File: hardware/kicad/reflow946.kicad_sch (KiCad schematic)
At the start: 47 parts, among them J1 VH-2A, J2 VH-3A2, J3 VH-3A2, J4 XH-A2, J5 HDR-M-2.54_2x3, Q1 BTA16-600BRG, Q2 MMBT3906, Q3 MMBT3906, Q4 MMBT3906, SW1 SW_Push, SW2 SW_Push, SW3 SW_Push, U1 MOC3041M, U2 ESP32-WROOM-32U, U3 MAX31855KASA, U4 AMS1117-3.3

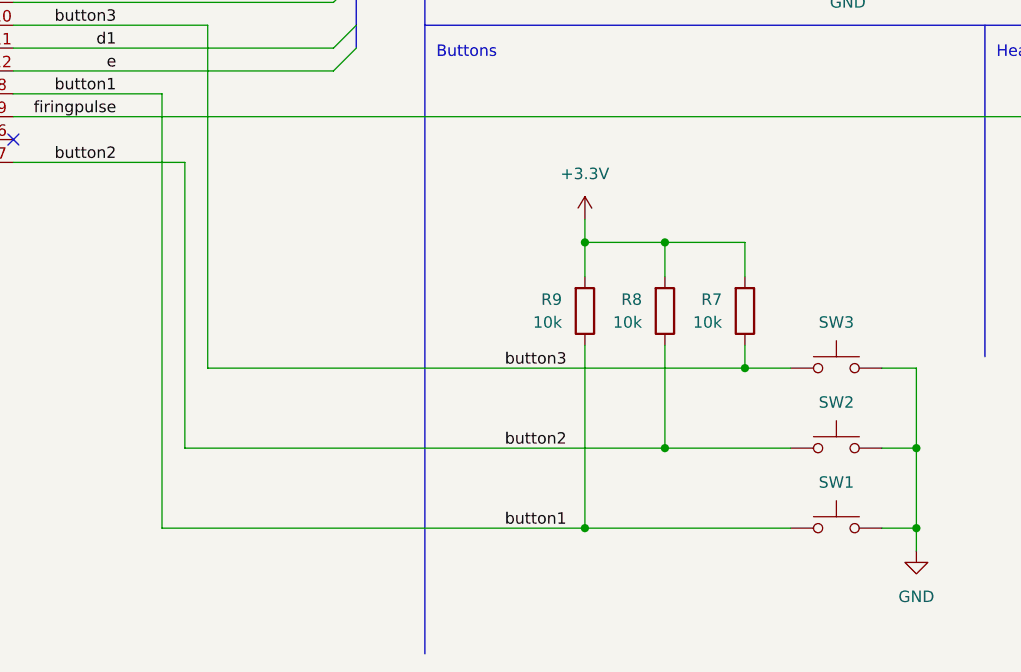
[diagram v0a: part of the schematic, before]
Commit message: Fix wrong pinout on push buttons
Leaving pull up resistor footprints in place, so they can be populated
if needed.
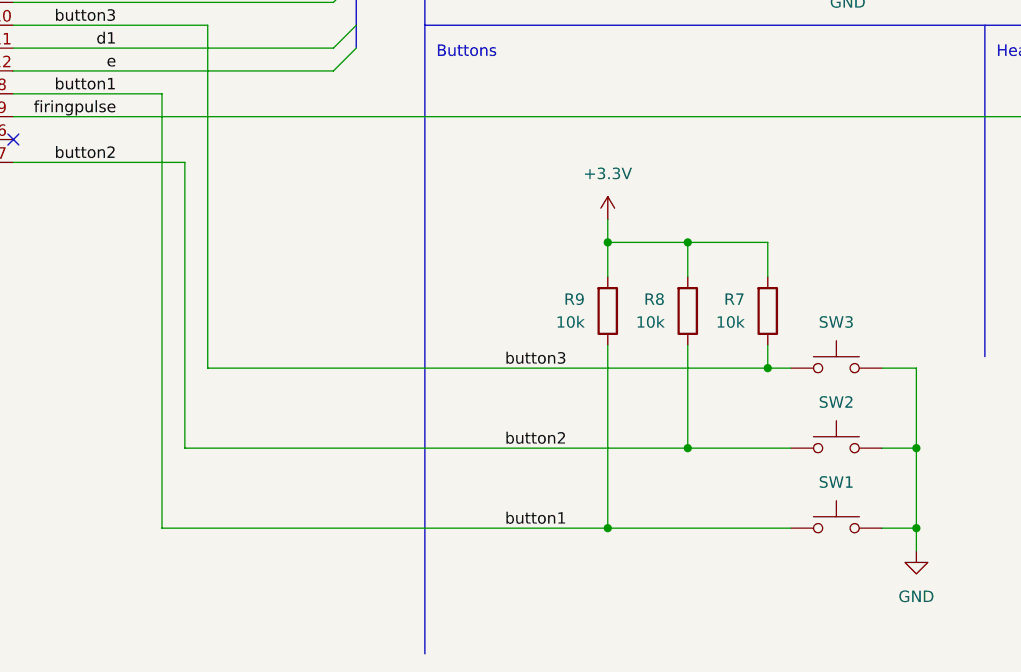
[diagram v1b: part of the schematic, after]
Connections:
- net GND: now also SW1.2, SW2.2, SW3.2; no longer SW1.1, SW2.1, SW3.1
- net button1: now also SW1.1; no longer SW1.2
- net button2: now also SW2.1; no longer SW2.2
- net button3: now also SW3.1; no longer SW3.2
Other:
- moved on the sheet: R7, R8, R9
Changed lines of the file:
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@@
     (company "Arnaud Durand")
   )
-  (junction (at 132.08 184.15) (diameter 0) (color 0 0 0 0)
-  )
-  (junction (at 132.08 152.4) (diameter 0) (color 0 0 0 0)
+  (junction (at 134.62 184.15) (diameter 0) (color 0 0 0 0)
+  )
+  (junction (at 134.62 152.4) (diameter 0) (color 0 0 0 0)
   )
   (junction (at 73.66 33.02) (diameter 0) (color 0 0 0 0)
   )
-  (junction (at 140.97 175.26) (diameter 0) (color 0 0 0 0)
+  (junction (at 143.51 175.26) (diameter 0) (color 0 0 0 0)
   )
   (junction (at 179.07 101.6) (diameter 0) (color 0 0 0 0)
@@
   (junction (at 27.94 85.09) (diameter 0) (color 0 0 0 0)
   )
-  (junction (at 149.86 166.37) (diameter 0) (color 0 0 0 0)
+  (junction (at 152.4 166.37) (diameter 0) (color 0 0 0 0)
   )
   (junction (at 209.55 22.86) (diameter 0) (color 0 0 0 0)
@@
   (junction (at 194.31 22.86) (diameter 0) (color 0 0 0 0)
   )
-  (junction (at 140.97 152.4) (diameter 0) (color 0 0 0 0)
+  (junction (at 143.51 152.4) (diameter 0) (color 0 0 0 0)
   )
   (junction (at 179.07 114.3) (diameter 0) (color 0 0 0 0)
@@
     (stroke (width 0) (type default) (color 0 0 0 0))
   )
-  (wire (pts (xy 132.08 184.15) (xy 85.09 184.15))
+  (wire (pts (xy 134.62 184.15) (xy 85.09 184.15))
     (stroke (width 0) (type default) (color 0 0 0 0))
   )
@@
     (stroke (width 0) (type default) (color 0 0 0 0))
   )
-  (wire (pts (xy 149.86 166.37) (xy 149.86 163.83))
+  (wire (pts (xy 152.4 166.37) (xy 152.4 163.83))
     (stroke (width 0) (type default) (color 0 0 0 0))
   )
@@
     (stroke (width 0) (type default) (color 0 0 0 0))
   )
-  (wire (pts (xy 140.97 152.4) (xy 140.97 156.21))
+  (wire (pts (xy 143.51 152.4) (xy 143.51 156.21))
     (stroke (width 0) (type default) (color 0 0 0 0))
   )
@@
     (stroke (width 0) (type default) (color 0 0 0 0))
   )
-  (wire (pts (xy 132.08 149.86) (xy 132.08 152.4))
+  (wire (pts (xy 134.62 149.86) (xy 134.62 152.4))
     (stroke (width 0) (type default) (color 0 0 0 0))
   )
@@
     (stroke (width 0) (type default) (color 0 0 0 0))
   )
-  (wire (pts (xy 140.97 152.4) (xy 132.08 152.4))
+  (wire (pts (xy 143.51 152.4) (xy 134.62 152.4))
     (stroke (width 0) (type default) (color 0 0 0 0))
   )
@@
     (stroke (width 0) (type default) (color 0 0 0 0))
   )
-  (wire (pts (xy 154.94 184.15) (xy 132.08 184.15))
+  (wire (pts (xy 154.94 184.15) (xy 134.62 184.15))
     (stroke (width 0) (type default) (color 0 0 0 0))
   )
@@
     (stroke (width 0) (type default) (color 0 0 0 0))
   )
-  (wire (pts (xy 154.94 175.26) (xy 140.97 175.26))
+  (wire (pts (xy 154.94 175.26) (xy 143.51 175.26))
     (stroke (width 0) (type default) (color 0 0 0 0))
   )
@@
     (stroke (width 0) (type default) (color 0 0 0 0))
   )
-  (wire (pts (xy 154.94 166.37) (xy 149.86 166.37))
+  (wire (pts (xy 154.94 166.37) (xy 152.4 166.37))
     (stroke (width 0) (type default) (color 0 0 0 0))
   )
@@
     (stroke (width 0) (type default) (color 0 0 0 0))
   )
-  (wire (pts (xy 132.08 156.21) (xy 132.08 152.4))
+  (wire (pts (xy 134.62 156.21) (xy 134.62 152.4))
     (stroke (width 0) (type default) (color 0 0 0 0))
   )
@@
     (stroke (width 0) (type default) (color 0 0 0 0))
   )
-  (wire (pts (xy 149.86 156.21) (xy 149.86 152.4))
+  (wire (pts (xy 152.4 156.21) (xy 152.4 152.4))
     (stroke (width 0) (type default) (color 0 0 0 0))
   )
@@
     (stroke (width 0) (type default) (color 0 0 0 0))
   )
-  (wire (pts (xy 140.97 175.26) (xy 87.63 175.26))
+  (wire (pts (xy 143.51 175.26) (xy 87.63 175.26))
     (stroke (width 0) (type default) (color 0 0 0 0))
   )
@@
     (stroke (width 0) (type default) (color 0 0 0 0))
   )
-  (wire (pts (xy 149.86 152.4) (xy 140.97 152.4))
+  (wire (pts (xy 152.4 152.4) (xy 143.51 152.4))
     (stroke (width 0) (type default) (color 0 0 0 0))
   )
@@
     (stroke (width 0) (type default) (color 0 0 0 0))
   )
-  (wire (pts (xy 132.08 184.15) (xy 132.08 163.83))
+  (wire (pts (xy 134.62 184.15) (xy 134.62 163.83))
     (stroke (width 0) (type default) (color 0 0 0 0))
   )
@@
     (stroke (width 0) (type default) (color 0 0 0 0))
   )
-  (wire (pts (xy 90.17 166.37) (xy 149.86 166.37))
+  (wire (pts (xy 90.17 166.37) (xy 152.4 166.37))
     (stroke (width 0) (type default) (color 0 0 0 0))
   )
@@
     (stroke (width 0) (type default) (color 0 0 0 0))
   )
-  (wire (pts (xy 140.97 163.83) (xy 140.97 175.26))
+  (wire (pts (xy 143.51 163.83) (xy 143.51 175.26))
     (stroke (width 0) (type default) (color 0 0 0 0))
   )
@@
     (pin "1")
   )
-  (symbol (lib_id "Device:R") (at 132.08 160.02 0) (mirror x) (unit 1)
-    (in_bom yes) (on_board yes) (fields_autoplaced)
-    (property "Reference" "R9" (id 0) (at 129.54 158.7499 0)
+  (symbol (lib_id "Device:R") (at 134.62 160.02 0) (mirror x) (unit 1)
+    (in_bom yes) (on_board yes) (fields_autoplaced)
+    (property "Reference" "R9" (id 0) (at 132.08 158.7499 0)
       (effects (font (size 1.27 1.27)) (justify right))
     )
-    (property "Value" "10k" (id 1) (at 129.54 161.2899 0)
+    (property "Value" "10k" (id 1) (at 132.08 161.2899 0)
       (effects (font (size 1.27 1.27)) (justify right))
     )
-    (property "Footprint" "Resistor_SMD:R_0603_1608Metric_Pad0.98x0.95mm_HandSolder" (id 2) (at 130.302 160.02 90)
-      (effects (font (size 1.27 1.27)) hide)
-    )
-    (property "Datasheet" "~" (id 3) (at 132.08 160.02 0)
+    (property "Footprint" "Resistor_SMD:R_0603_1608Metric_Pad0.98x0.95mm_HandSolder" (id 2) (at 132.842 160.02 90)
+      (effects (font (size 1.27 1.27)) hide)
+    )
+    (property "Datasheet" "~" (id 3) (at 134.62 160.02 0)
       (effects (font (size 1.27 1.27)) hide)
     )
@@
     (pin "1")
   )
-  (symbol (lib_id "Device:R") (at 140.97 160.02 0) (mirror x) (unit 1)
-    (in_bom yes) (on_board yes) (fields_autoplaced)
-    (property "Reference" "R8" (id 0) (at 138.43 158.7499 0)
+  (symbol (lib_id "Device:R") (at 143.51 160.02 0) (mirror x) (unit 1)
+    (in_bom yes) (on_board yes) (fields_autoplaced)
+    (property "Reference" "R8" (id 0) (at 140.97 158.7499 0)
       (effects (font (size 1.27 1.27)) (justify right))
     )
-    (property "Value" "10k" (id 1) (at 138.43 161.2899 0)
+    (property "Value" "10k" (id 1) (at 140.97 161.2899 0)
       (effects (font (size 1.27 1.27)) (justify right))
     )
-    (property "Footprint" "Resistor_SMD:R_0603_1608Metric_Pad0.98x0.95mm_HandSolder" (id 2) (at 139.192 160.02 90)
-      (effects (font (size 1.27 1.27)) hide)
-    )
-    (property "Datasheet" "~" (id 3) (at 140.97 160.02 0)
+    (property "Footprint" "Resistor_SMD:R_0603_1608Metric_Pad0.98x0.95mm_HandSolder" (id 2) (at 141.732 160.02 90)
+      (effects (font (size 1.27 1.27)) hide)
+    )
+    (property "Datasheet" "~" (id 3) (at 143.51 160.02 0)
       (effects (font (size 1.27 1.27)) hide)
     )
@@
     (pin "9")
   )
-  (symbol (lib_id "Switch:SW_Push") (at 160.02 184.15 0) (mirror y) (unit 1)
+  (symbol (lib_id "Switch:SW_Push") (at 160.02 184.15 0) (unit 1)
     (in_bom yes) (on_board yes) (fields_autoplaced)
     (property "Reference" "SW1" (id 0) (at 160.02 179.07 0))
@@
     (pin "1")
   )
-  (symbol (lib_id "Device:R") (at 149.86 160.02 0) (mirror x) (unit 1)
-    (in_bom yes) (on_board yes) (fields_autoplaced)
-    (property "Reference" "R7" (id 0) (at 147.32 158.7499 0)
+  (symbol (lib_id "Device:R") (at 152.4 160.02 0) (mirror x) (unit 1)
+    (in_bom yes) (on_board yes) (fields_autoplaced)
+    (property "Reference" "R7" (id 0) (at 149.86 158.7499 0)
       (effects (font (size 1.27 1.27)) (justify right))
     )
-    (property "Value" "10k" (id 1) (at 147.32 161.2899 0)
+    (property "Value" "10k" (id 1) (at 149.86 161.2899 0)
       (effects (font (size 1.27 1.27)) (justify right))
     )
-    (property "Footprint" "Resistor_SMD:R_0603_1608Metric_Pad0.98x0.95mm_HandSolder" (id 2) (at 148.082 160.02 90)
-      (effects (font (size 1.27 1.27)) hide)
-    )
-    (property "Datasheet" "~" (id 3) (at 149.86 160.02 0)
-      (effects (font (size 1.27 1.27)) hide)
-    )
-    (pin "1")
-    (pin "2")
-  )
-  (symbol (lib_id "Switch:SW_Push") (at 160.02 175.26 0) (mirror y) (unit 1)
+    (property "Footprint" "Resistor_SMD:R_0603_1608Metric_Pad0.98x0.95mm_HandSolder" (id 2) (at 150.622 160.02 90)
+      (effects (font (size 1.27 1.27)) hide)
+    )
+    (property "Datasheet" "~" (id 3) (at 152.4 160.02 0)
+      (effects (font (size 1.27 1.27)) hide)
+    )
+    (pin "1")
+    (pin "2")
+  )
+  (symbol (lib_id "Switch:SW_Push") (at 160.02 175.26 0) (unit 1)
     (in_bom yes) (on_board yes) (fields_autoplaced)
     (property "Reference" "SW2" (id 0) (at 160.02 170.18 0))
@@
     (pin "2")
   )
-  (symbol (lib_id "power:+3.3V") (at 132.08 149.86 0) (mirror y) (unit 1)
-    (in_bom yes) (on_board yes) (fields_autoplaced)
-    (property "Reference" "#PWR0111" (id 0) (at 132.08 153.67 0)
-      (effects (font (size 1.27 1.27)) hide)
-    )
-    (property "Value" "+3.3V" (id 1) (at 132.08 144.78 0))
-    (property "Footprint" "" (id 2) (at 132.08 149.86 0)
-      (effects (font (size 1.27 1.27)) hide)
-    )
-    (property "Datasheet" "" (id 3) (at 132.08 149.86 0)
+  (symbol (lib_id "power:+3.3V") (at 134.62 149.86 0) (mirror y) (unit 1)
+    (in_bom yes) (on_board yes) (fields_autoplaced)
+    (property "Reference" "#PWR0111" (id 0) (at 134.62 153.67 0)
+      (effects (font (size 1.27 1.27)) hide)
+    )
+    (property "Value" "+3.3V" (id 1) (at 134.62 144.78 0))
+    (property "Footprint" "" (id 2) (at 134.62 149.86 0)
+      (effects (font (size 1.27 1.27)) hide)
+    )
+    (property "Datasheet" "" (id 3) (at 134.62 149.86 0)
       (effects (font (size 1.27 1.27)) hide)
     )
@@
     (pin "1")
   )
-  (symbol (lib_id "Switch:SW_Push") (at 160.02 166.37 0) (mirror y) (unit 1)
+  (symbol (lib_id "Switch:SW_Push") (at 160.02 166.37 0) (unit 1)
     (in_bom yes) (on_board yes) (fields_autoplaced)
     (property "Reference" "SW3" (id 0) (at 160.02 161.29 0))

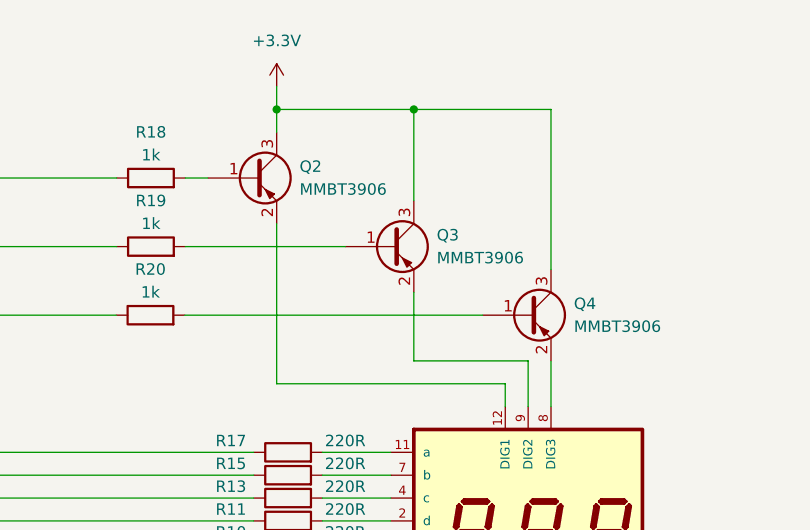
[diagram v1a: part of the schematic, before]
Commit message: Fix PNP transistors missplacement
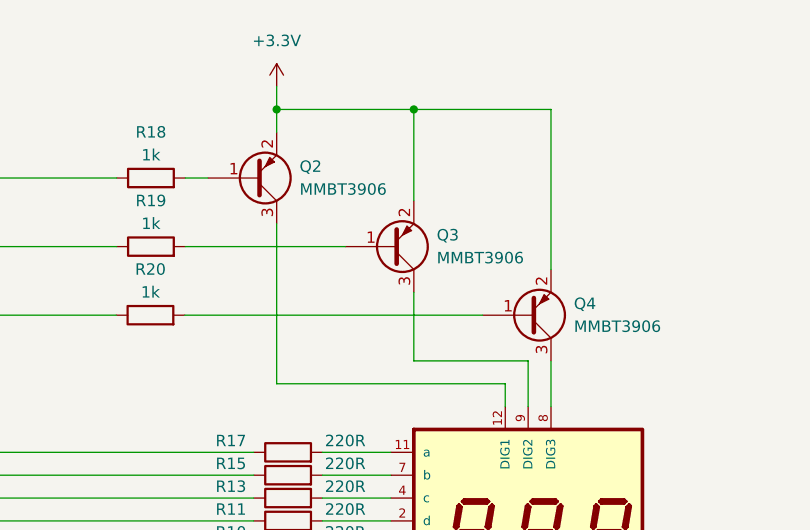
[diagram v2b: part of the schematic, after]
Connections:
- net +3.3V: now also Q2.2 (E), Q3.2 (E), Q4.2 (E); no longer Q2.3 (C), Q3.3 (C), Q4.3 (C)
- net at DS1.12 (DIG1): now also Q2.3 (C); no longer Q2.2 (E)
- net at DS1.8 (DIG3): now also Q4.3 (C); no longer Q4.2 (E)
- net at DS1.9 (DIG2): now also Q3.3 (C); no longer Q3.2 (E)
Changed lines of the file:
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@@
     (pin "2")
   )
-  (symbol (lib_id "Transistor_BJT:MMBT3906") (at 222.25 45.72 0) (unit 1)
+  (symbol (lib_id "Transistor_BJT:MMBT3906") (at 222.25 45.72 0) (mirror x) (unit 1)
     (in_bom yes) (on_board yes) (fields_autoplaced)
     (property "Reference" "Q4" (id 0) (at 227.33 44.4499 0)
@@
       (effects (font (size 1.27 1.27)) (justify left))
     )
-    (property "Footprint" "Package_TO_SOT_SMD:SOT-23" (id 2) (at 227.33 47.625 0)
+    (property "Footprint" "Package_TO_SOT_SMD:SOT-23" (id 2) (at 227.33 43.815 0)
       (effects (font (size 1.27 1.27) italic) (justify left) hide)
     )
@@
     (pin "2")
   )
-  (symbol (lib_id "Transistor_BJT:MMBT3906") (at 207.01 38.1 0) (unit 1)
+  (symbol (lib_id "Transistor_BJT:MMBT3906") (at 207.01 38.1 0) (mirror x) (unit 1)
     (in_bom yes) (on_board yes) (fields_autoplaced)
     (property "Reference" "Q3" (id 0) (at 212.09 36.8299 0)
@@
       (effects (font (size 1.27 1.27)) (justify left))
     )
-    (property "Footprint" "Package_TO_SOT_SMD:SOT-23" (id 2) (at 212.09 40.005 0)
+    (property "Footprint" "Package_TO_SOT_SMD:SOT-23" (id 2) (at 212.09 36.195 0)
       (effects (font (size 1.27 1.27) italic) (justify left) hide)
     )
@@
     (pin "2")
   )
-  (symbol (lib_id "Transistor_BJT:MMBT3906") (at 191.77 30.48 0) (unit 1)
+  (symbol (lib_id "Transistor_BJT:MMBT3906") (at 191.77 30.48 0) (mirror x) (unit 1)
     (in_bom yes) (on_board yes) (fields_autoplaced)
     (property "Reference" "Q2" (id 0) (at 196.85 29.2099 0)
@@
       (effects (font (size 1.27 1.27)) (justify left))
     )
-    (property "Footprint" "Package_TO_SOT_SMD:SOT-23" (id 2) (at 196.85 32.385 0)
+    (property "Footprint" "Package_TO_SOT_SMD:SOT-23" (id 2) (at 196.85 28.575 0)
       (effects (font (size 1.27 1.27) italic) (justify left) hide)
     )

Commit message: Use 0603 ferrite beads
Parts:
- FB1, FB2: footprint Resistor_SMD:R_0402_1005Metric_Pad0.72x0.64mm_HandSolder -> Resistor_SMD:R_0603_1608Metric_Pad0.98x0.95mm_HandSolder
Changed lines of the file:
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@@
       (effects (font (size 1.27 1.27)) hide)
     )
-    (property "Footprint" "Resistor_SMD:R_0402_1005Metric_Pad0.72x0.64mm_HandSolder" (id 2) (at 193.04 116.078 90)
+    (property "Footprint" "Resistor_SMD:R_0603_1608Metric_Pad0.98x0.95mm_HandSolder" (id 2) (at 193.04 116.078 90)
       (effects (font (size 1.27 1.27)) hide)
     )
@@
       (effects (font (size 1.27 1.27)) hide)
     )
-    (property "Footprint" "Resistor_SMD:R_0402_1005Metric_Pad0.72x0.64mm_HandSolder" (id 2) (at 193.04 103.378 90)
+    (property "Footprint" "Resistor_SMD:R_0603_1608Metric_Pad0.98x0.95mm_HandSolder" (id 2) (at 193.04 103.378 90)
       (effects (font (size 1.27 1.27)) hide)
     )
@@
     )
     (path "/5092413b-b3a7-4468-a8a4-dae7a08665ca"
-      (reference "FB1") (unit 1) (value "FerriteBead") (footprint "Resistor_SMD:R_0402_1005Metric_Pad0.72x0.64mm_HandSolder")
+      (reference "FB1") (unit 1) (value "FerriteBead") (footprint "Resistor_SMD:R_0603_1608Metric_Pad0.98x0.95mm_HandSolder")
     )
     (path "/ecc49533-7a2f-4586-9bbf-23096fabfb73"
-      (reference "FB2") (unit 1) (value "FerriteBead") (footprint "Resistor_SMD:R_0402_1005Metric_Pad0.72x0.64mm_HandSolder")
+      (reference "FB2") (unit 1) (value "FerriteBead") (footprint "Resistor_SMD:R_0603_1608Metric_Pad0.98x0.95mm_HandSolder")
     )
     (path "/aefaf454-2975-4b97-a001-c5e7b8345189"
